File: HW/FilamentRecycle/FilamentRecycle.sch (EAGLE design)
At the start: 22 parts, among them CON5 MOLEX-53261-0671, IC1 ATMEGA48A-AU, IC7 FT232RL, Q1 16MHz, Q2 BC847ALT1SMD, Q3 BC847ALT1SMD, X6 PN61729-S

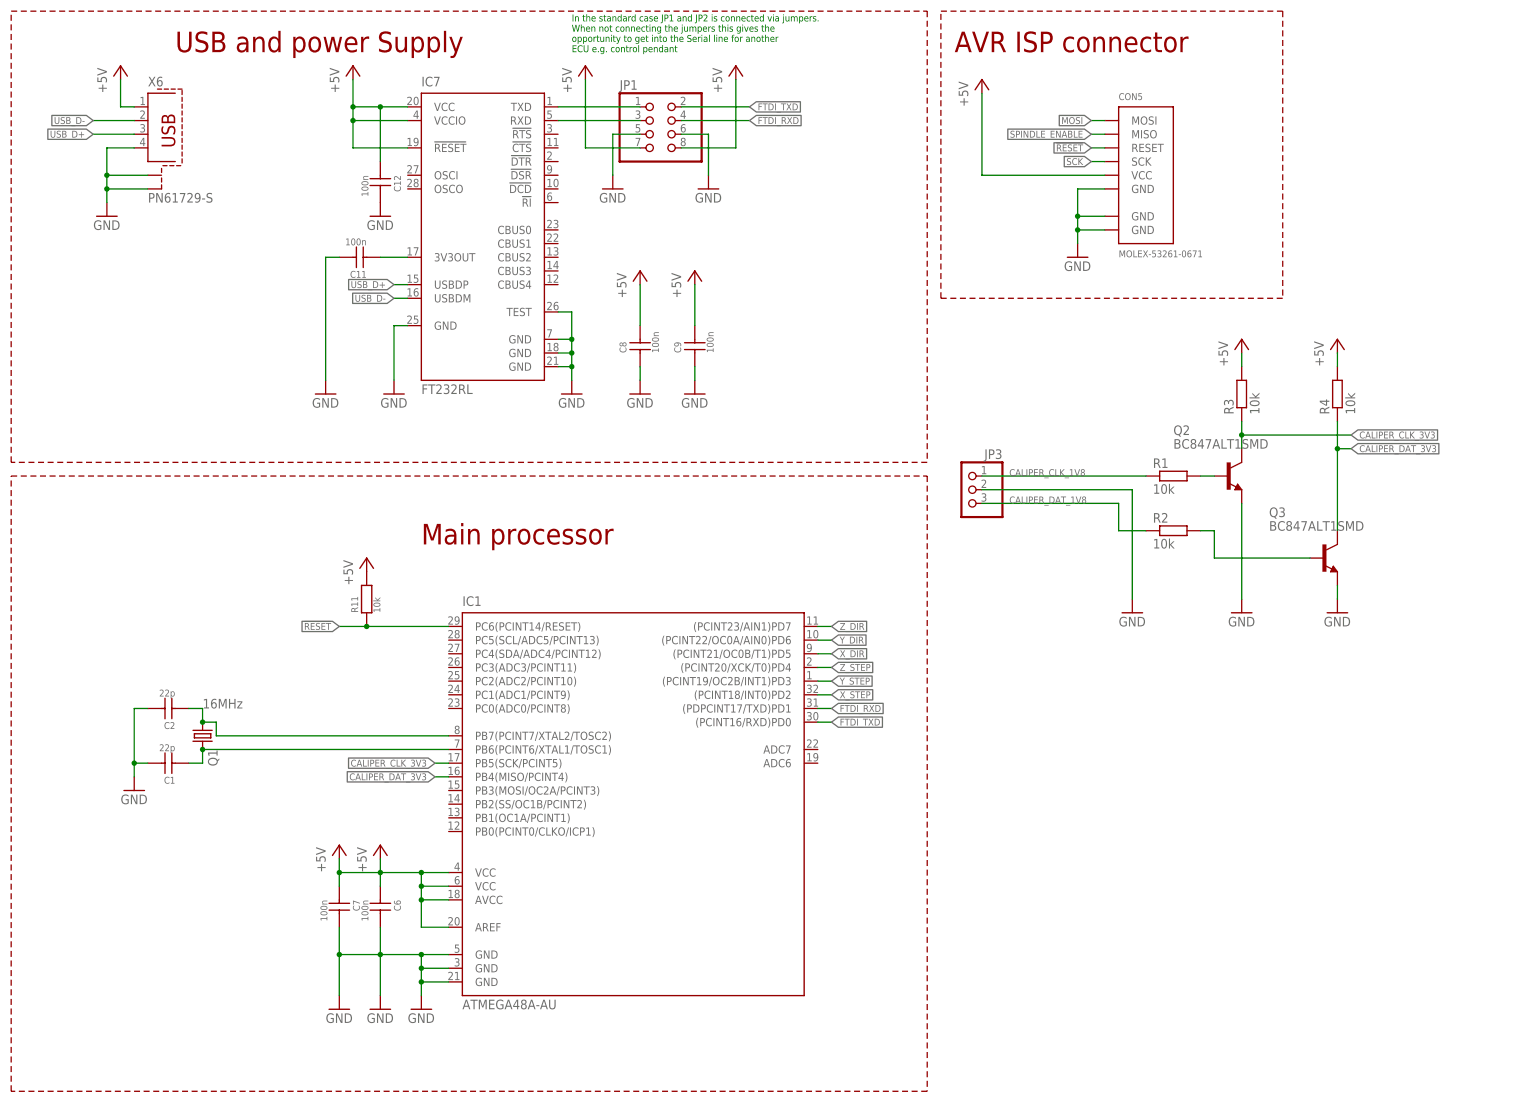
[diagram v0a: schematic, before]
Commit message: Reading the caliper via uart working
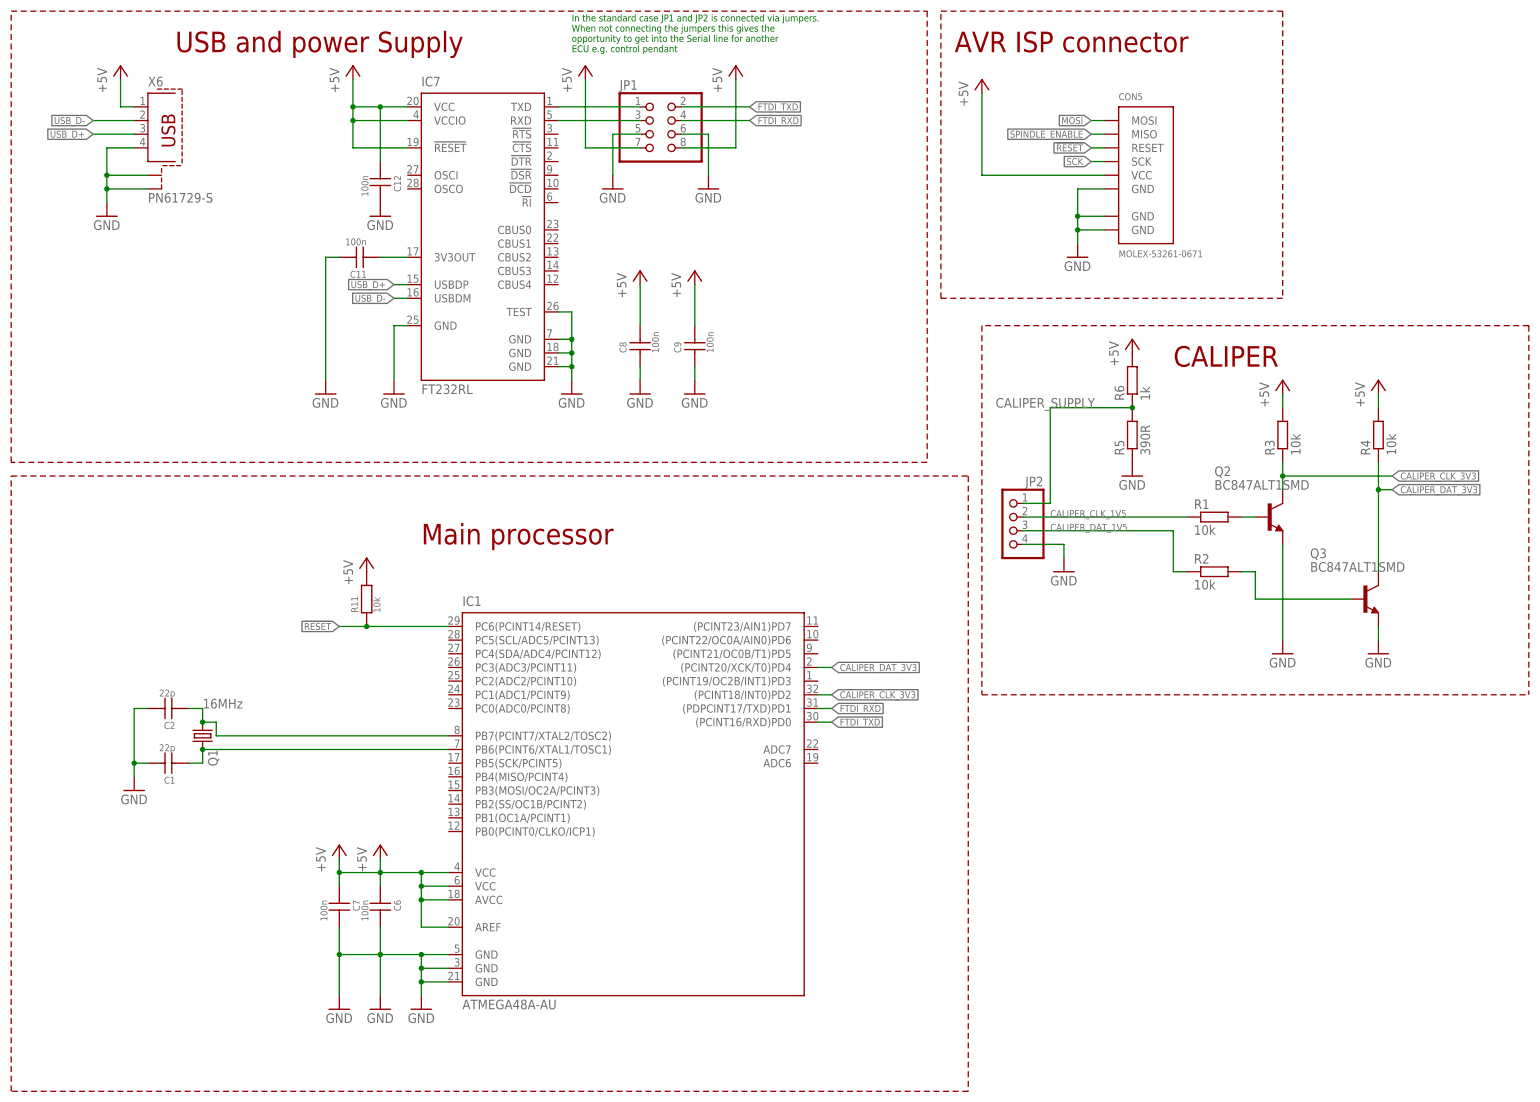
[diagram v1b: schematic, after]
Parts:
- removed JP3: (no value), pinhead:PINHD-1X3
- added JP2: (no value), pinhead:PINHD-1X4
- added R5: 390R, rcl:R-EU_R0603
- added R6: 1k, rcl:R-EU_R0603
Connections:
- removed net CALIPER_CLK_1V8: JP3.1, R1.1
- removed net CALIPER_DAT_1V8: JP3.3, R2.1
- removed net X_DIR: IC1.(PCINT21/OC0B/T1)PD5
- removed net X_STEP: IC1.(PCINT18/INT0)PD2
- removed net Y_DIR: IC1.(PCINT22/OC0A/AIN0)PD6
- removed net Y_STEP: IC1.(PCINT19/OC2B/INT1)PD3
- removed net Z_DIR: IC1.(PCINT23/AIN1)PD7
- removed net Z_STEP: IC1.(PCINT20/XCK/T0)PD4
- new net CALIPER_CLK_1V5: JP2.2, R1.1
- new net CALIPER_DAT_1V5: JP2.3, R2.1
- new net CALIPER_SUPPLY: JP2.1, R5.2, R6.1
- net +5V: now also R6.2
- net CALIPER_CLK_3V3: now also IC1.(PCINT18/INT0)PD2; no longer IC1.PB5(SCK/PCINT5)
- net CALIPER_DAT_3V3: now also IC1.(PCINT20/XCK/T0)PD4; no longer IC1.PB4(MISO/PCINT4)
- net GND: now also JP2.4, R5.1; no longer JP3.2
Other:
- note added: "CALIPER"
- moved on the sheet: Q2, Q3, R1, R2, R3, R4

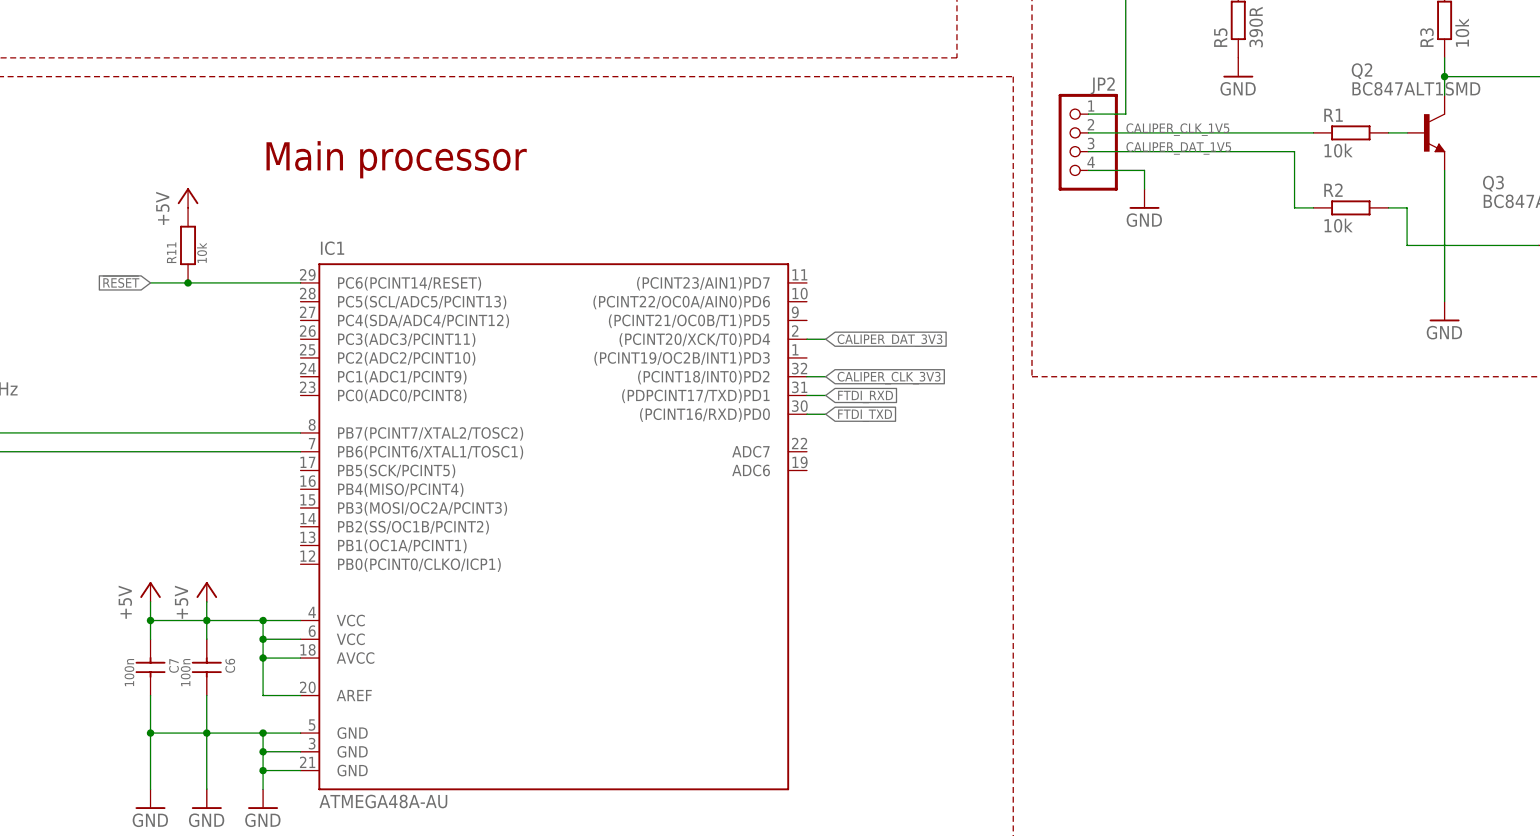
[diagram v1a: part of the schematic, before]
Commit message: first version of NTC handling
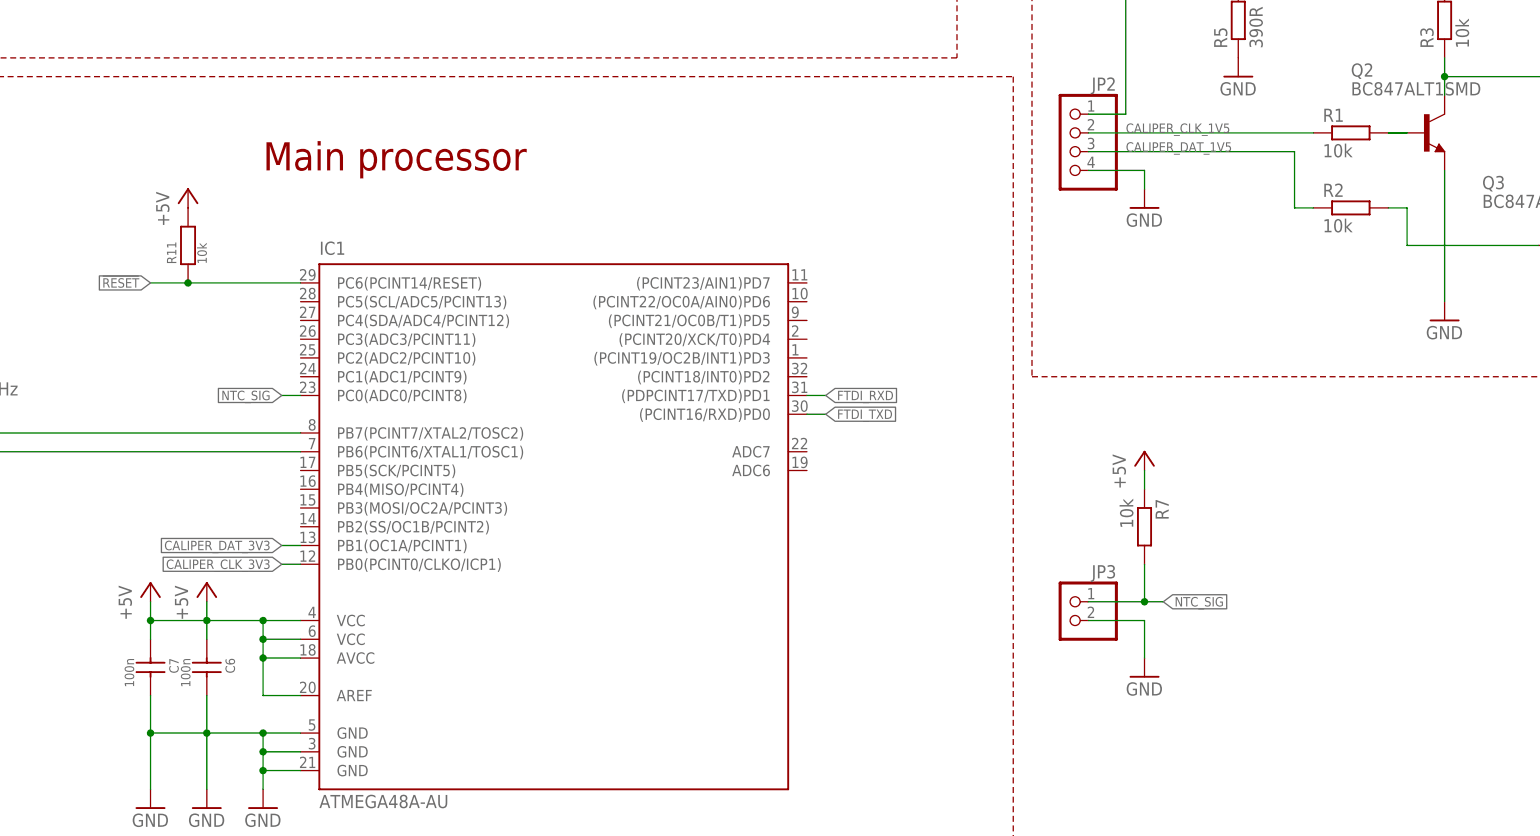
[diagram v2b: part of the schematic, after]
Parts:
- added JP3: (no value), pinhead:PINHD-1X2
- added R7: 10k, rcl:R-EU_R0603
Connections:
- new net NTC_SIG: IC1.PC0(ADC0/PCINT8), JP3.1, R7.2
- net +5V: now also R7.1
- net CALIPER_CLK_3V3: now also IC1.PB0(PCINT0/CLKO/ICP1); no longer IC1.(PCINT18/INT0)PD2
- net CALIPER_DAT_3V3: now also IC1.PB1(OC1A/PCINT1); no longer IC1.(PCINT20/XCK/T0)PD4
- net GND: now also JP3.2
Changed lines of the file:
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@@
 <part name="U$5" library="SchlegelAr_Master" deviceset="+5V" device=""/>
 <part name="GND14" library="supply1" deviceset="GND" device=""/>
+<part name="JP3" library="pinhead" deviceset="PINHD-1X2" device=""/>
+<part name="GND15" library="supply1" deviceset="GND" device=""/>
+<part name="R7" library="rcl" deviceset="R-EU_" device="R0603" value="10k"/>
+<part name="U$6" library="SchlegelAr_Master" deviceset="+5V" device=""/>
 </parts>
 <sheets>
@@
 <instance part="U$5" gate="G$1" x="210.82" y="144.78"/>
 <instance part="GND14" gate="1" x="210.82" y="121.92"/>
+<instance part="JP3" gate="G$1" x="187.96" y="48.26" rot="MR0"/>
+<instance part="GND15" gate="1" x="198.12" y="40.64"/>
+<instance part="R7" gate="G$1" x="198.12" y="60.96" rot="R270"/>
+<instance part="U$6" gate="G$1" x="198.12" y="68.58"/>
 </instances>
 <busses>
@@
 <pinref part="R5" gate="G$1" pin="1"/>
 <pinref part="GND14" gate="1" pin="GND"/>
+</segment>
+<segment>
+<pinref part="JP3" gate="G$1" pin="2"/>
+<pinref part="GND15" gate="1" pin="GND"/>
+<wire x1="190.5" y1="48.26" x2="198.12" y2="48.26" width="0.1524" layer="91"/>
+<wire x1="198.12" y1="48.26" x2="198.12" y2="43.18" width="0.1524" layer="91"/>
 </segment>
 </net>
@@
 <pinref part="U$5" gate="G$1" pin="+5V"/>
 </segment>
+<segment>
+<pinref part="R7" gate="G$1" pin="1"/>
+<pinref part="U$6" gate="G$1" pin="+5V"/>
+<wire x1="198.12" y1="68.58" x2="198.12" y2="66.04" width="0.1524" layer="91"/>
+</segment>
 </net>
 <net name="FTDI_TXD" class="0">
@@
 <net name="CALIPER_CLK_3V3" class="0">
 <segment>
-<label x="154.94" y="81.28" size="1.27" layer="95" xref="yes"/>
-<wire x1="152.4" y1="81.28" x2="154.94" y2="81.28" width="0.1524" layer="91"/>
-<pinref part="IC1" gate="G$1" pin="(PCINT18/INT0)PD2"/>
+<label x="81.28" y="55.88" size="1.27" layer="95" rot="R180" xref="yes"/>
+<wire x1="83.82" y1="55.88" x2="81.28" y2="55.88" width="0.1524" layer="91"/>
+<pinref part="IC1" gate="G$1" pin="PB0(PCINT0/CLKO/ICP1)"/>
 </segment>
 <segment>
@@
 <net name="CALIPER_DAT_3V3" class="0">
 <segment>
-<label x="154.94" y="86.36" size="1.27" layer="95" xref="yes"/>
-<wire x1="152.4" y1="86.36" x2="154.94" y2="86.36" width="0.1524" layer="91"/>
-<pinref part="IC1" gate="G$1" pin="(PCINT20/XCK/T0)PD4"/>
+<label x="81.28" y="58.42" size="1.27" layer="95" rot="R180" xref="yes"/>
+<wire x1="83.82" y1="58.42" x2="81.28" y2="58.42" width="0.1524" layer="91"/>
+<pinref part="IC1" gate="G$1" pin="PB1(OC1A/PCINT1)"/>
 </segment>
 <segment>
@@
 <pinref part="Q2" gate="G$1" pin="B"/>
 <pinref part="R1" gate="G$1" pin="2"/>
+<wire x1="233.68" y1="114.3" x2="231.14" y2="114.3" width="0.1524" layer="91"/>
 <wire x1="233.68" y1="114.3" x2="231.14" y2="114.3" width="0.1524" layer="91"/>
 </segment>
@@
 </segment>
 </net>
+<net name="NTC_SIG" class="0">
+<segment>
+<pinref part="IC1" gate="G$1" pin="PC0(ADC0/PCINT8)"/>
+<wire x1="83.82" y1="78.74" x2="81.28" y2="78.74" width="0.1524" layer="91"/>
+<label x="81.28" y="78.74" size="1.27" layer="95" rot="R180" xref="yes"/>
+</segment>
+<segment>
+<pinref part="JP3" gate="G$1" pin="1"/>
+<wire x1="190.5" y1="50.8" x2="198.12" y2="50.8" width="0.1524" layer="91"/>
+<pinref part="R7" gate="G$1" pin="2"/>
+<wire x1="198.12" y1="50.8" x2="198.12" y2="55.88" width="0.1524" layer="91"/>
+<wire x1="198.12" y1="50.8" x2="200.66" y2="50.8" width="0.1524" layer="91"/>
+<junction x="198.12" y="50.8"/>
+<label x="200.66" y="50.8" size="1.27" layer="95" xref="yes"/>
+</segment>
+</net>
